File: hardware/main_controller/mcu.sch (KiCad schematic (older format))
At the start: 32 parts, among them SW1 SW_Push, U1 STM32F407V(E-G)Tx_u, Y1 8MHz

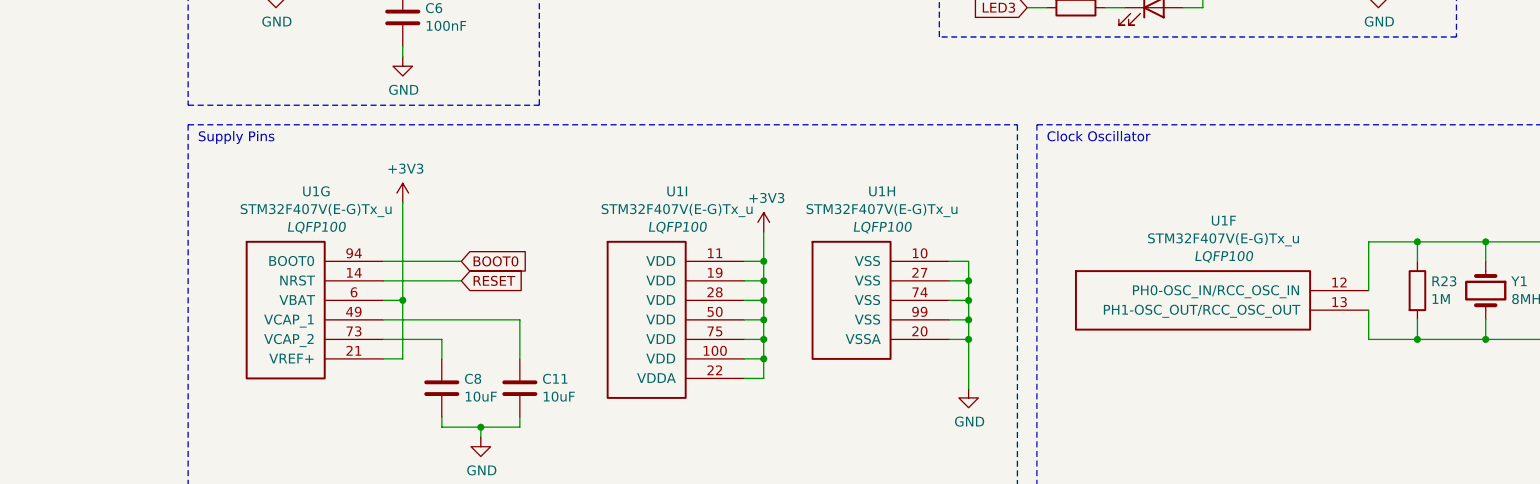
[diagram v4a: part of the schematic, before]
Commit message: assigned footprints
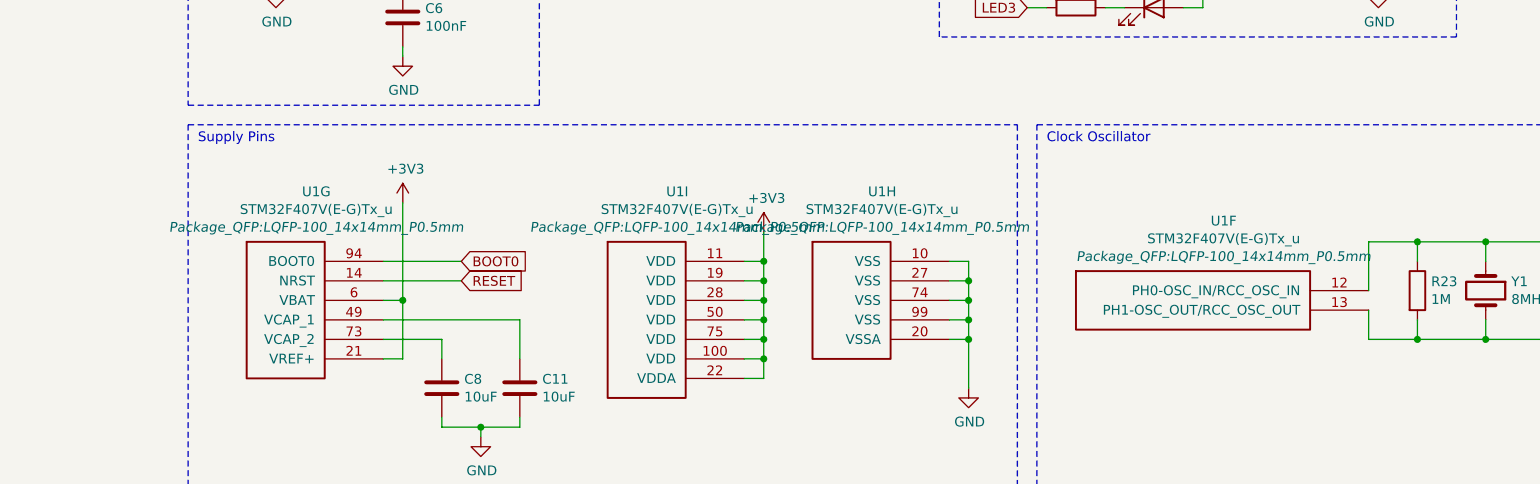
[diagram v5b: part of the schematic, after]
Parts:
- C10, C12, C13, C15, C16, C2, C3, C4, C5, C6, C7, C9: footprint (none) -> Capacitor_SMD:C_0201_0603Metric
- C11, C14, C8: footprint (none) -> Capacitor_Tantalum_SMD:CP_EIA-3216-10_Kemet-I
- D1, D2, D3, D4, D5: footprint (none) -> LED_SMD:LED_0603_1608Metric
- R15, R16, R17, R18, R19, R20, R21, R22, R23: footprint (none) -> Resistor_SMD:R_0201_0603Metric
- SW1: footprint (none) -> Button_Switch_SMD:SW_Push_1P1T-SH_NO_CK_KMR2xxG
- U1: footprint LQFP100 -> Package_QFP:LQFP-100_14x14mm_P0.5mm
- Y1: footprint (none) -> Crystal:Crystal_SMD_5032-4Pin_5.0x3.2mm
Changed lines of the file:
@@
 F 0 "U1" H 4057 3757 50  0000 C CNN
 F 1 "STM32F407V(E-G)Tx_u" H 4057 3666 50  0000 C CNN
-F 2 "LQFP100" H 4057 3575 50  0000 C CIN
+F 2 "Package_QFP:LQFP-100_14x14mm_P0.5mm" H 4057 3575 50  0000 C CIN
 F 3 "" H 3900 3100 50  0000 C CNN
 	7    3900 3100
@@
 F 0 "R16" H 6620 946 50  0000 L CNN
 F 1 "10K" H 6620 855 50  0000 L CNN
-F 2 "" V 6480 900 50  0001 C CNN
+F 2 "Resistor_SMD:R_0201_0603Metric" V 6480 900 50  0001 C CNN
 F 3 "~" H 6550 900 50  0001 C CNN
 	1    6550 900
@@
 F 0 "R17" H 6920 946 50  0000 L CNN
 F 1 "10k" H 6920 855 50  0000 L CNN
-F 2 "" V 6780 900 50  0001 C CNN
+F 2 "Resistor_SMD:R_0201_0603Metric" V 6780 900 50  0001 C CNN
 F 3 "~" H 6850 900 50  0001 C CNN
 	1    6850 900
@@
 F 0 "SW1" H 4150 1585 50  0000 C CNN
 F 1 "SW_Push" H 4150 1494 50  0000 C CNN
-F 2 "" H 4150 1500 50  0001 C CNN
+F 2 "Button_Switch_SMD:SW_Push_1P1T-SH_NO_CK_KMR2xxG" H 4150 1500 50  0001 C CNN
 F 3 "~" H 4150 1500 50  0001 C CNN
 	1    4150 1300
@@
 F 0 "R15" H 4570 1096 50  0000 L CNN
 F 1 "10k" H 4570 1005 50  0000 L CNN
-F 2 "" V 4430 1050 50  0001 C CNN
+F 2 "Resistor_SMD:R_0201_0603Metric" V 4430 1050 50  0001 C CNN
 F 3 "~" H 4500 1050 50  0001 C CNN
 	1    4500 1050
@@
 F 0 "C6" H 4615 1596 50  0000 L CNN
 F 1 "100nF" H 4615 1505 50  0000 L CNN
-F 2 "" H 4538 1400 50  0001 C CNN
+F 2 "Capacitor_SMD:C_0201_0603Metric" H 4538 1400 50  0001 C CNN
 F 3 "~" H 4500 1550 50  0001 C CNN
 	1    4500 1550
@@
 F 0 "R20" V 7743 1500 50  0000 C CNN
 F 1 "510" V 7834 1500 50  0000 C CNN
-F 2 "" V 7880 1500 50  0001 C CNN
+F 2 "Resistor_SMD:R_0201_0603Metric" V 7880 1500 50  0001 C CNN
 F 3 "~" H 7950 1500 50  0001 C CNN
 	1    7950 1500
@@
 F 0 "R19" V 7743 1200 50  0000 C CNN
 F 1 "510" V 7834 1200 50  0000 C CNN
-F 2 "" V 7880 1200 50  0001 C CNN
+F 2 "Resistor_SMD:R_0201_0603Metric" V 7880 1200 50  0001 C CNN
 F 3 "~" H 7950 1200 50  0001 C CNN
 	1    7950 1200
@@
 F 0 "R18" V 7743 900 50  0000 C CNN
 F 1 "510" V 7834 900 50  0000 C CNN
-F 2 "" V 7880 900 50  0001 C CNN
+F 2 "Resistor_SMD:R_0201_0603Metric" V 7880 900 50  0001 C CNN
 F 3 "~" H 7950 900 50  0001 C CNN
 	1    7950 900
@@
 F 0 "D1" H 8343 1117 50  0000 C CNN
 F 1 "LED" H 8343 1026 50  0000 C CNN
-F 2 "" H 8350 900 50  0001 C CNN
+F 2 "LED_SMD:LED_0603_1608Metric" H 8350 900 50  0001 C CNN
 F 3 "~" H 8350 900 50  0001 C CNN
 	1    8350 900
@@
 F 0 "D2" H 8343 1417 50  0000 C CNN
 F 1 "LED" H 8343 1326 50  0000 C CNN
-F 2 "" H 8350 1200 50  0001 C CNN
+F 2 "LED_SMD:LED_0603_1608Metric" H 8350 1200 50  0001 C CNN
 F 3 "~" H 8350 1200 50  0001 C CNN
 	1    8350 1200
@@
 F 0 "D3" H 8343 1717 50  0000 C CNN
 F 1 "LED" H 8343 1626 50  0000 C CNN
-F 2 "" H 8350 1500 50  0001 C CNN
+F 2 "LED_SMD:LED_0603_1608Metric" H 8350 1500 50  0001 C CNN
 F 3 "~" H 8350 1500 50  0001 C CNN
 	1    8350 1500
@@
 F 0 "D4" H 8843 645 50  0000 C CNN
 F 1 "LED" H 8843 736 50  0000 C CNN
-F 2 "" H 8850 900 50  0001 C CNN
+F 2 "LED_SMD:LED_0603_1608Metric" H 8850 900 50  0001 C CNN
 F 3 "~" H 8850 900 50  0001 C CNN
 	1    8850 900
@@
 F 0 "D5" H 8843 945 50  0000 C CNN
 F 1 "LED" H 8843 1036 50  0000 C CNN
-F 2 "" H 8850 1200 50  0001 C CNN
+F 2 "LED_SMD:LED_0603_1608Metric" H 8850 1200 50  0001 C CNN
 F 3 "~" H 8850 1200 50  0001 C CNN
 	1    8850 1200
@@
 F 0 "R21" V 9043 900 50  0000 C CNN
 F 1 "510" V 9134 900 50  0000 C CNN
-F 2 "" V 9180 900 50  0001 C CNN
+F 2 "Resistor_SMD:R_0201_0603Metric" V 9180 900 50  0001 C CNN
 F 3 "~" H 9250 900 50  0001 C CNN
 	1    9250 900
@@
 F 0 "R22" V 9043 1200 50  0000 C CNN
 F 1 "510" V 9134 1200 50  0000 C CNN
-F 2 "" V 9180 1200 50  0001 C CNN
+F 2 "Resistor_SMD:R_0201_0603Metric" V 9180 1200 50  0001 C CNN
 F 3 "~" H 9250 1200 50  0001 C CNN
 	1    9250 1200
@@
 F 0 "U1" H 6957 3557 50  0000 C CNN
 F 1 "STM32F407V(E-G)Tx_u" H 6957 3466 50  0000 C CNN
-F 2 "LQFP100" H 6957 3375 50  0000 C CIN
+F 2 "Package_QFP:LQFP-100_14x14mm_P0.5mm" H 6957 3375 50  0000 C CIN
 F 3 "" H 6800 3000 50  0000 C CNN
 	8    6800 3000
@@
 F 0 "U1" H 5907 3757 50  0000 C CNN
 F 1 "STM32F407V(E-G)Tx_u" H 5907 3666 50  0000 C CNN
-F 2 "LQFP100" H 5907 3575 50  0000 C CIN
+F 2 "Package_QFP:LQFP-100_14x14mm_P0.5mm" H 5907 3575 50  0000 C CIN
 F 3 "" H 5750 3100 50  0000 C CNN
 	9    5750 3100
@@
 F 0 "C8" H 4815 3496 50  0000 L CNN
 F 1 "10uF" H 4815 3405 50  0000 L CNN
-F 2 "" H 4738 3300 50  0001 C CNN
+F 2 "Capacitor_Tantalum_SMD:CP_EIA-3216-10_Kemet-I" H 4738 3300 50  0001 C CNN
 F 3 "~" H 4700 3450 50  0001 C CNN
 	1    4700 3450
@@
 F 0 "C11" H 5215 3496 50  0000 L CNN
 F 1 "10uF" H 5215 3405 50  0000 L CNN
-F 2 "" H 5138 3300 50  0001 C CNN
+F 2 "Capacitor_Tantalum_SMD:CP_EIA-3216-10_Kemet-I" H 5138 3300 50  0001 C CNN
 F 3 "~" H 5100 3450 50  0001 C CNN
 	1    5100 3450
@@
 F 0 "C2" H 3865 4646 50  0000 L CNN
 F 1 "100nF" H 3865 4555 50  0000 L CNN
-F 2 "" H 3788 4450 50  0001 C CNN
+F 2 "Capacitor_SMD:C_0201_0603Metric" H 3788 4450 50  0001 C CNN
 F 3 "~" H 3750 4600 50  0001 C CNN
 	1    3750 4600
@@
 F 0 "C3" H 4065 4646 50  0000 L CNN
 F 1 "100nF" H 4065 4555 50  0000 L CNN
-F 2 "" H 3988 4450 50  0001 C CNN
+F 2 "Capacitor_SMD:C_0201_0603Metric" H 3988 4450 50  0001 C CNN
 F 3 "~" H 3950 4600 50  0001 C CNN
 	1    3950 4600
@@
 F 0 "C4" H 4265 4646 50  0000 L CNN
 F 1 "100nF" H 4265 4555 50  0000 L CNN
-F 2 "" H 4188 4450 50  0001 C CNN
+F 2 "Capacitor_SMD:C_0201_0603Metric" H 4188 4450 50  0001 C CNN
 F 3 "~" H 4150 4600 50  0001 C CNN
 	1    4150 4600
@@
 F 0 "C5" H 4465 4646 50  0000 L CNN
 F 1 "100nF" H 4465 4555 50  0000 L CNN
-F 2 "" H 4388 4450 50  0001 C CNN
+F 2 "Capacitor_SMD:C_0201_0603Metric" H 4388 4450 50  0001 C CNN
 F 3 "~" H 4350 4600 50  0001 C CNN
 	1    4350 4600
@@
 F 0 "C13" H 5465 4646 50  0000 L CNN
 F 1 "100nF" H 5465 4555 50  0000 L CNN
-F 2 "" H 5388 4450 50  0001 C CNN
+F 2 "Capacitor_SMD:C_0201_0603Metric" H 5388 4450 50  0001 C CNN
 F 3 "~" H 5350 4600 50  0001 C CNN
 	1    5350 4600
@@
 F 0 "C12" H 5265 4646 50  0000 L CNN
 F 1 "100nF" H 5265 4555 50  0000 L CNN
-F 2 "" H 5188 4450 50  0001 C CNN
+F 2 "Capacitor_SMD:C_0201_0603Metric" H 5188 4450 50  0001 C CNN
 F 3 "~" H 5150 4600 50  0001 C CNN
 	1    5150 4600
@@
 F 0 "C10" H 5065 4646 50  0000 L CNN
 F 1 "100nF" H 5065 4555 50  0000 L CNN
-F 2 "" H 4988 4450 50  0001 C CNN
+F 2 "Capacitor_SMD:C_0201_0603Metric" H 4988 4450 50  0001 C CNN
 F 3 "~" H 4950 4600 50  0001 C CNN
 	1    4950 4600
@@
 F 0 "C9" H 4865 4646 50  0000 L CNN
 F 1 "100nF" H 4865 4555 50  0000 L CNN
-F 2 "" H 4788 4450 50  0001 C CNN
+F 2 "Capacitor_SMD:C_0201_0603Metric" H 4788 4450 50  0001 C CNN
 F 3 "~" H 4750 4600 50  0001 C CNN
 	1    4750 4600
@@
 F 0 "C7" H 4665 4646 50  0000 L CNN
 F 1 "100nF" H 4665 4555 50  0000 L CNN
-F 2 "" H 4588 4450 50  0001 C CNN
+F 2 "Capacitor_SMD:C_0201_0603Metric" H 4588 4450 50  0001 C CNN
 F 3 "~" H 4550 4600 50  0001 C CNN
 	1    4550 4600
@@
 F 0 "C14" H 5968 4646 50  0000 L CNN
 F 1 "10uF" H 5968 4555 50  0000 L CNN
-F 2 "" H 5888 4450 50  0001 C CNN
+F 2 "Capacitor_Tantalum_SMD:CP_EIA-3216-10_Kemet-I" H 5888 4450 50  0001 C CNN
 F 3 "~" H 5850 4600 50  0001 C CNN
 	1    5850 4600
@@
 F 0 "C16" V 10248 3200 50  0000 C CNN
 F 1 "22pF" V 10339 3200 50  0000 C CNN
-F 2 "" H 10538 3050 50  0001 C CNN
+F 2 "Capacitor_SMD:C_0201_0603Metric" H 10538 3050 50  0001 C CNN
 F 3 "~" H 10500 3200 50  0001 C CNN
 	1    10500 3200
@@
 F 0 "C15" V 10248 2700 50  0000 C CNN
 F 1 "22pF" V 10339 2700 50  0000 C CNN
-F 2 "" H 10538 2550 50  0001 C CNN
+F 2 "Capacitor_SMD:C_0201_0603Metric" H 10538 2550 50  0001 C CNN
 F 3 "~" H 10500 2700 50  0001 C CNN
 	1    10500 2700
@@
 F 0 "R23" H 9770 2996 50  0000 L CNN
 F 1 "1M" H 9770 2905 50  0000 L CNN
-F 2 "" V 9630 2950 50  0001 C CNN
+F 2 "Resistor_SMD:R_0201_0603Metric" V 9630 2950 50  0001 C CNN
 F 3 "~" H 9700 2950 50  0001 C CNN
 	1    9700 2950
@@
 F 0 "Y1" V 10004 3081 50  0000 L CNN
 F 1 "8MHz" V 10095 3081 50  0000 L CNN
-F 2 "" H 10050 2950 50  0001 C CNN
+F 2 "Crystal:Crystal_SMD_5032-4Pin_5.0x3.2mm" H 10050 2950 50  0001 C CNN
 F 3 "~" H 10050 2950 50  0001 C CNN
 	1    10050 2950
@@
 F 0 "U1" H 8707 3507 50  0000 C CNN
 F 1 "STM32F407V(E-G)Tx_u" H 8707 3416 50  0000 C CNN
-F 2 "LQFP100" H 8707 3325 50  0000 C CIN
+F 2 "Package_QFP:LQFP-100_14x14mm_P0.5mm" H 8707 3325 50  0000 C CIN
 F 3 "" H 8550 3050 50  0000 C CNN
 	6    8550 3050
